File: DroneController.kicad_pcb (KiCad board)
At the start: 4 copper layers, 50.7 x 56.1 mm, 81 parts, among them J1 Connector, J2 Connector, J3 Connector, J4 UART Flash, J5 UART Flash, P1 USB_C_Plug, Q2 AO3400A, Q3 AO3400A, U1 ICM-42605, U2 W25Q16JVSS, U3 BMP280, U4 MPU-6500, U5 STM32F411, U6 L86-M33, U7 915MHz, U9 AP7361C-33E, X1 Shenzhen SCTF Elec SX2B12.000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

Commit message: Finalized PCB and layout of MKII of Drone Controller
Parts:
- removed C1: 10nF, PCM_JLCPCB:C_0402
- removed C2, C3: 100nF, PCM_JLCPCB:C_0402
- removed J1, J2, J3: Connector, TerminalBlock:TerminalBlock_MaiXu_MX126-5.0-02P_1x02_P5.00mm
- removed J4, J5: UART Flash, Connector_PinHeader_1.00mm:PinHeader_1x03_P1.00mm_Vertical
- removed R10: 5.1kΩ, PCM_JLCPCB:R_0402
- removed the R9 at (113.0, 121.8)
- removed the REF** at (104.2, 157.9)
- removed the REF** at (62.2, 26.1)
- removed the REF** at (148.4, 108.7)
- removed the REF** at (104.0, 147.2)
- removed SHOUHAN-SPDT: SPDT, SW-SHOUHAN_MST-22D18G23J_C2875122:SPDT
- removed TP1 (x2): TestPoint, TestPoint:TestPoint_Pad_1.0x1.0mm
- removed TP5, TP9: TestPoint, TestPoint:TestPoint_Keystone_5019_Miniature
- removed U4: MPU-6500, MPU-6500:QFN24_3X3X0P9_IVS
- added BATT: Connector, easyeda2kicad:CONN-TH_B2B-XH-A-LF-SN, F.Cu at (112.0, 54.4)
- added LIPO: Connector, easyeda2kicad:CONN-TH_B2B-XH-A-LF-SN, F.Cu at (64.5, 64.6)
- added REF**: TestPoint_Pad_1.0x1.0mm, TestPoint:TestPoint_Pad_1.0x1.0mm, F.Cu at (71.4, 74.8)
- added REF**: TestPoint_Pad_1.0x1.0mm, TestPoint:TestPoint_Pad_1.0x1.0mm, F.Cu at (71.4, 72.6)
- added REF**: MountingHole_2.1mm, MountingHole:MountingHole_2.1mm, F.Cu at (64.8, 72.8)
- added REF**: PinHeader_1x04_P1.27mm_Vertical, Connector_PinHeader_1.27mm:PinHeader_1x04_P1.27mm_Vertical, F.Cu at (69.9, 62.8)
- added REF**: MountingHole_2.1mm, MountingHole:MountingHole_2.1mm, F.Cu at (113.2, 73.2)
- added RESET: TS1101S, easyeda2kicad:SW-SMD_4P-L4.5-W4.5-P3.15-LS7.5-TL, F.Cu at (102.2, 46.6)
- added SWD: Conn_01x04_Pin, Connector_PinHeader_1.00mm:PinHeader_1x04_P1.00mm_Vertical, F.Cu at (63.0, 52.2)
- added UART: Conn_01x04_Pin, Connector_PinHeader_1.00mm:PinHeader_1x04_P1.00mm_Vertical, F.Cu at (63.0, 57.4)
- added UART2: Connector, easyeda2kicad:CONN-TH_B2B-XH-A-LF-SN, F.Cu at (112.0, 62.8)
- moved REF** 158.7 mm to (64.2, 23.4)
- moved REF** 80.5 mm to (79.6, 30.6)
- moved REF** 80.5 mm to (81.8, 30.6)
- moved G*** 70.0 mm to (108.9, 71.3)
- moved R5 55.2 mm to (105.2, 42.0), turned to -90 degrees
- moved D5 52.1 mm to (103.5, 41.8), turned to -90 degrees
- moved Q2 46.7 mm to (100.6, 41.6), turned to 90 degrees
- moved MOSI1 15.1 mm to (76.0, 26.2), turned to 180 degrees
- moved BOOT 14.9 mm to (101.8, 69.2), turned to 0 degrees
- moved SCK1 12.1 mm to (76.0, 29.4), turned to 0 degrees
- moved MISO1 10.7 mm to (76.0, 23.0), turned to 180 degrees
- moved C5 10.0 mm to (66.6, 35.4), turned to 0 degrees
- moved U9 8.68 mm to (66.0, 30.4), turned to 90 degrees
- moved C4 7.90 mm to (68.5, 35.4), turned to 180 degrees
- moved MOSI2 5.00 mm to (77.6, 34.8), turned to 0 degrees
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- renumbered SHOUHAN-SPDT to BOOT, TP2 to MISO1, TP6 to MISO2, TP3 to MOSI1, TP7 to MOSI2, TP4 to SCK1, TP8 to SCK2
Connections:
- P1 pad A6: unconnected-(P1-DP1-PadA6) -> /USB_FS_DP
- P1 pad B7: unconnected-(P1-DN2-PadB7) -> /USB_FS_DN
- Q2 pad 1: /SWCLK -> Net-(Q2-G)
- REF** pad 1: Net-(U5-NRST) -> Net-(U2-~{HOLD}/~{RESET}/IO_{3})
- U2 pad 2: /SPI1_MOSI -> /SPI1_MISO
- U2 pad 5: /SPI1_MISO -> /SPI1_MOSI
- U5 pad 11: /ADC1 -> Net-(Q2-G)
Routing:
- net +3.3V: track 101.4 -> 48.8 mm, vias 2 -> 38
- net +BATT: track 7.83 -> 51.1 mm, vias 1 -> 2
- net GND: track 92.0 -> 130.0 mm, vias 48 -> 47
- net /MCU_RX2: track 1.15 -> 37.7 mm
- net /MCU_TX2: track 1.19 -> 34.2 mm
- net Net-(SW2-B): track 0.00 -> 25.4 mm
- net /Debug_RX: track 3.07 -> 26.5 mm
- net Net-(U6-~{RESET}): track 0.00 -> 15.0 mm
- net /SPI2_SCK: track 6.40 -> 17.0 mm
- net Net-(Q2-G): track 0.00 -> 10.0 mm
- net Net-(D1-K): track 13.8 -> 4.91 mm
- net /SPI5_NSS: track 3.25 -> 11.0 mm, vias 1 -> 2
- net /IMU_INT: track 3.15 -> 10.9 mm, vias 1 -> 2
- net /SPI2_MISO: track 3.79 -> 10.5 mm, vias 0 -> 2
- net /SPI2_MOSI: track 4.85 -> 11.0 mm, vias 0 -> 2
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- added copper zone on F.Cu, net +3.3V
- added copper zone on In2.Cu, net +3.3V
- removed copper zone on In2.Cu, net GND
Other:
- board size 50.7 x 56.1 mm -> 54.6 x 55.4 mm
- board text added: "RESET"
- board text added: "This is the MK II of the AmmarAndEvan Flight Computer. This is a joint interdisciplinary project in which we build a FPV Drone. More iterations will follow."
- board text removed: "BOOT"
- board text removed: "COINCELL"
- board text removed: "J2"
- board text removed: "LIPO"
- board text removed: "This is the MK I of the AmmarAndEvan Flight Computer. This is a joint interdisciplinary project in which we build a FPV Drone. More iterations will follow."
- board text removed: "U4"
- board text removed: "U5"
- board text removed: "UART"
- board text removed: "X1"

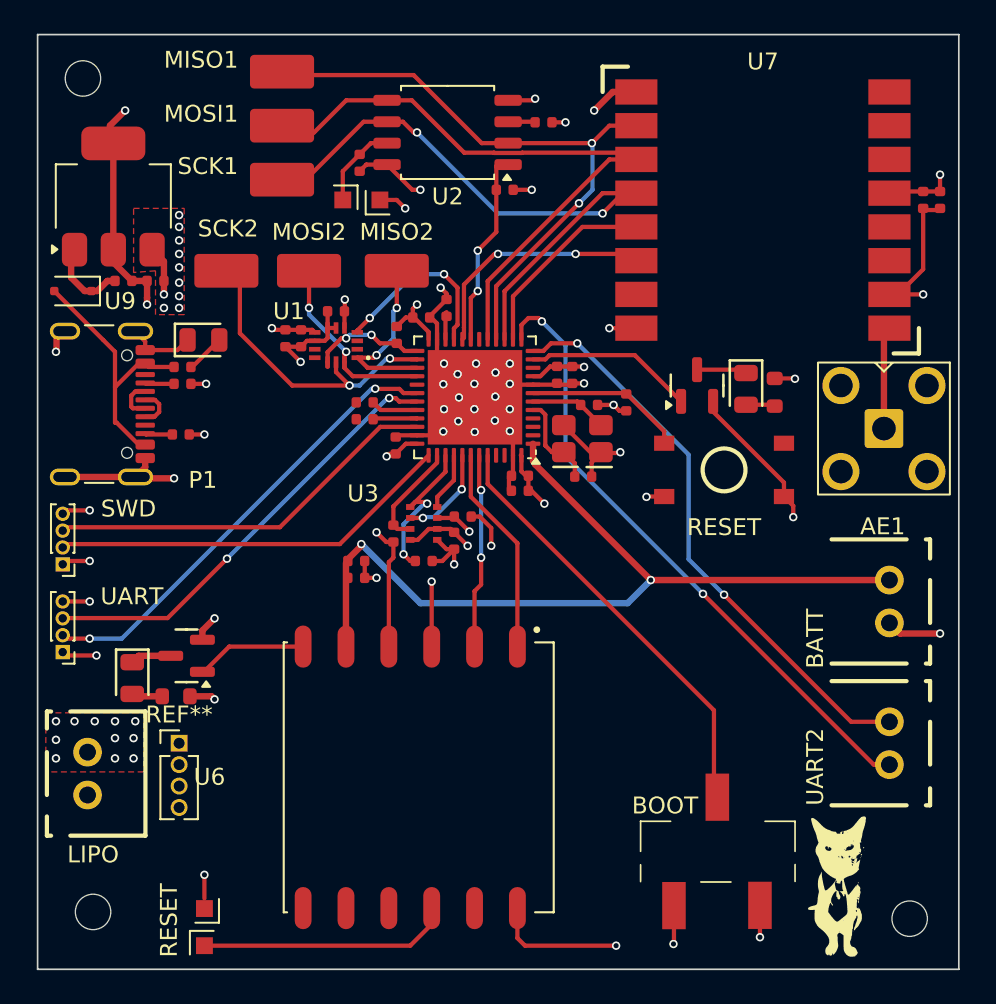
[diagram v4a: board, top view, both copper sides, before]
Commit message: Finalized MK II of drone controller, added 3D models, followed PCBWay DRC.
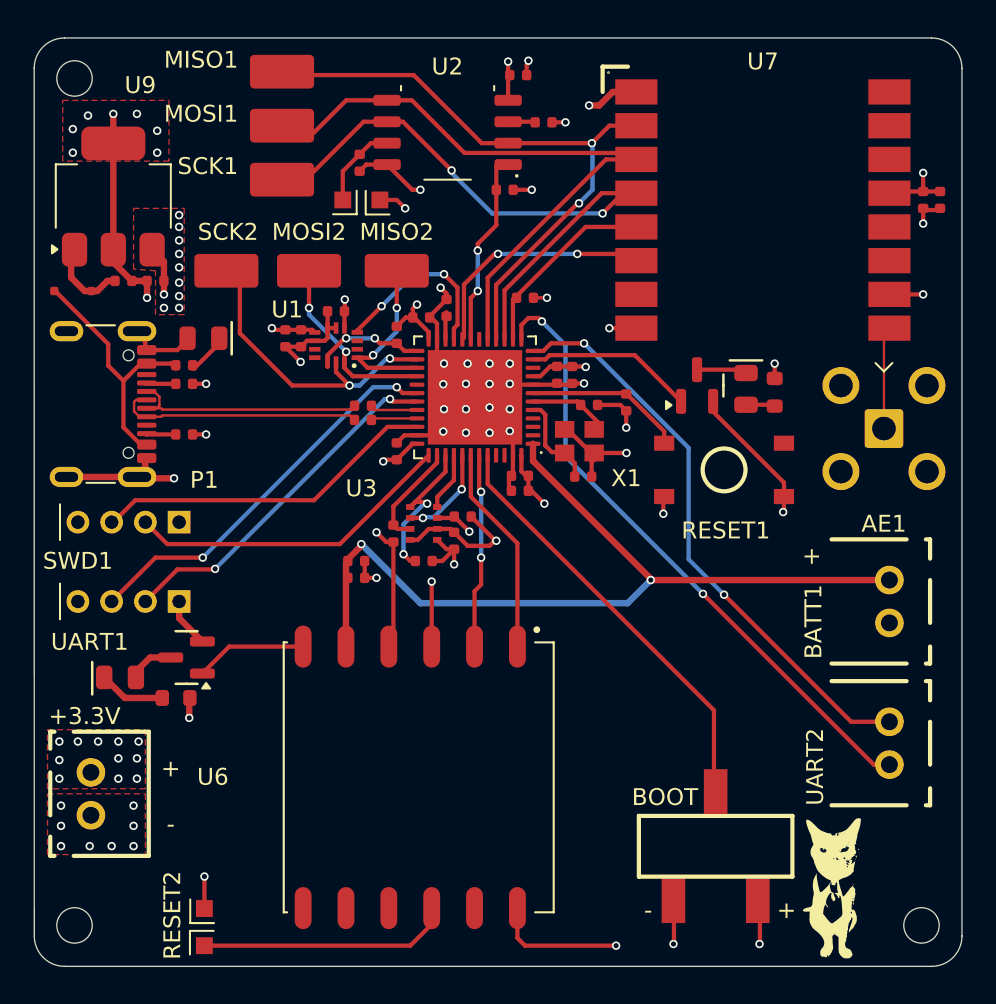
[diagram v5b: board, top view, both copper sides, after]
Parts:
- removed the BOOT at (101.8, 69.2)
- removed C14: 10uF, PCM_JLCPCB:C_0402
- removed the REF** at (69.9, 62.8)
- added BOOT: SW_SPDT, SW-SHOUHAN_MST-22D18G23J_C2875122:SW-SMD_SHOUHAN_MST-22D18G23J_C2875122, F.Cu at (101.7, 68.9)
- added C1: 100nF, PCM_JLCPCB:C_0402, F.Cu at (90.0, 23.2)
- added C3: 10uF, PCM_JLCPCB:C_0402, F.Cu at (114.0, 30.6)
- added G***: LOGO, LOGO, B.Cu at (77.3, 24.1)
- added R10: 5.1kΩ, PCM_JLCPCB:R_0402, F.Cu at (90.4, 36.4)
- SWD1: renamed from SWD; footprint Connector_PinHeader_1.00mm:PinHeader_1x04_P1.00mm_Vertical -> Connector_PinHeader_2.00mm:PinHeader_1x04_P2.00mm_Vertical
- UART1: renamed from UART; footprint Connector_PinHeader_1.00mm:PinHeader_1x04_P1.00mm_Vertical -> Connector_PinHeader_2.00mm:PinHeader_1x04_P2.00mm_Vertical
- X1: footprint PCM_JLCPCB:CRYSTAL-SMD_4P-L3.2-W2.5-BL -> Crystal:Crystal_SMD_2520-4Pin_2.5x2.0mm
- moved UART1 7.52 mm to (69.9, 54.4), turned to -90 degrees
- moved SWD1 7.34 mm to (69.9, 49.7), turned to -90 degrees
- moved REF** 1.36 mm to (63.7, 73.6)
- moved +3.3V 1.22 mm to (64.7, 65.8)
- moved REF** 0.81 mm to (113.9, 73.6)
- moved D6 0.72 mm to (66.4, 58.9), turned to 180 degrees
- moved REF** 0.50 mm to (63.7, 23.4)
- moved C29 0.35 mm to (82.8, 45.5)
- moved G*** 0.32 mm to (108.6, 71.4)
- moved X1 0.23 mm to (93.6, 44.9)
- moved R6 0.22 mm to (80.8, 42.8)
- moved R2 0.20 mm to (70.2, 44.5)
- moved R11 0.14 mm to (70.2, 40.4)
- moved R14 0.11 mm to (80.8, 43.6)
- moved R1 0.10 mm to (70.2, 41.5)
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- renumbered LIPO to +3.3V, BATT to BATT1, RESET to RESET1
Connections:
- C20 pad 1: 3.3V -> +3.3V
- C21 pad 1: 3.3V -> +3.3V
- U5 pad 18: /SPI5_SCK -> unconnected-(U5-PB0-Pad18)
- U5 pad 9: 3.3V -> +3.3V
- UART1 pad 2: /Debug_TX -> /Debug_RX
- UART1 pad 3: /Debug_RX -> /Debug_TX
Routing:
- net /USB_FS_DP: track 2.34 -> 14.7 mm
- net /USB_FS_DN: track 2.45 -> 14.7 mm
- net GND: track 130.0 -> 120.5 mm, vias 47 -> 54
- net /Debug_RX: track 26.5 -> 21.1 mm
- net /SWCLK: track 24.0 -> 19.5 mm
- net /Debug_TX: track 27.3 -> 23.5 mm
- net 3.3V: track 3.27 -> 0.00 mm, vias 1 -> 0
- net /SWDIO: track 23.5 -> 20.8 mm
- net Net-(D6-Pad2): track 1.84 -> 3.95 mm
- net +3.3V: track 48.8 -> 50.8 mm, vias 38 -> 39
- net +5V: track 15.8 -> 15.3 mm
- added copper zone on F.Cu, net GND
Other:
- board size 54.6 x 55.4 mm -> 55 x 55 mm
- board text added: "+"
- board text added: "-"
- board text added: "CLK"
- board text added: "DIO"
- board text added: "RESET2"
- board text added: "RX"
- board text added: "TX"
- board text added: "This is the MK II of the Open Source Drone Flight Computer. More iterations will follow."
- board text removed: "RESET"
- board text removed: "This is the MK II of the AmmarAndEvan Flight Computer. This is a joint interdisciplinary project in which we build a FPV Drone. More iterations will follow."
